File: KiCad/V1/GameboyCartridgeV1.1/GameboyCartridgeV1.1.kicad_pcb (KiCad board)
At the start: 4 copper layers, 52.8 x 61.2 mm, 52 parts, among them J1 USB_C_Receptacle_USB2.0, J2 DBG_UART, J3 Conn_01x06, Q1 CJ2302, SW1 SW_Push, U2 W25Q128JVS, U3 RP2040, U4 CartBus, U5 MCP1825T-3302E/DC, U6 TXB0102DCU, U7 TXB0108PW, U8 TXB0108PW, U9 TXB0108PW, Y1 12MHz

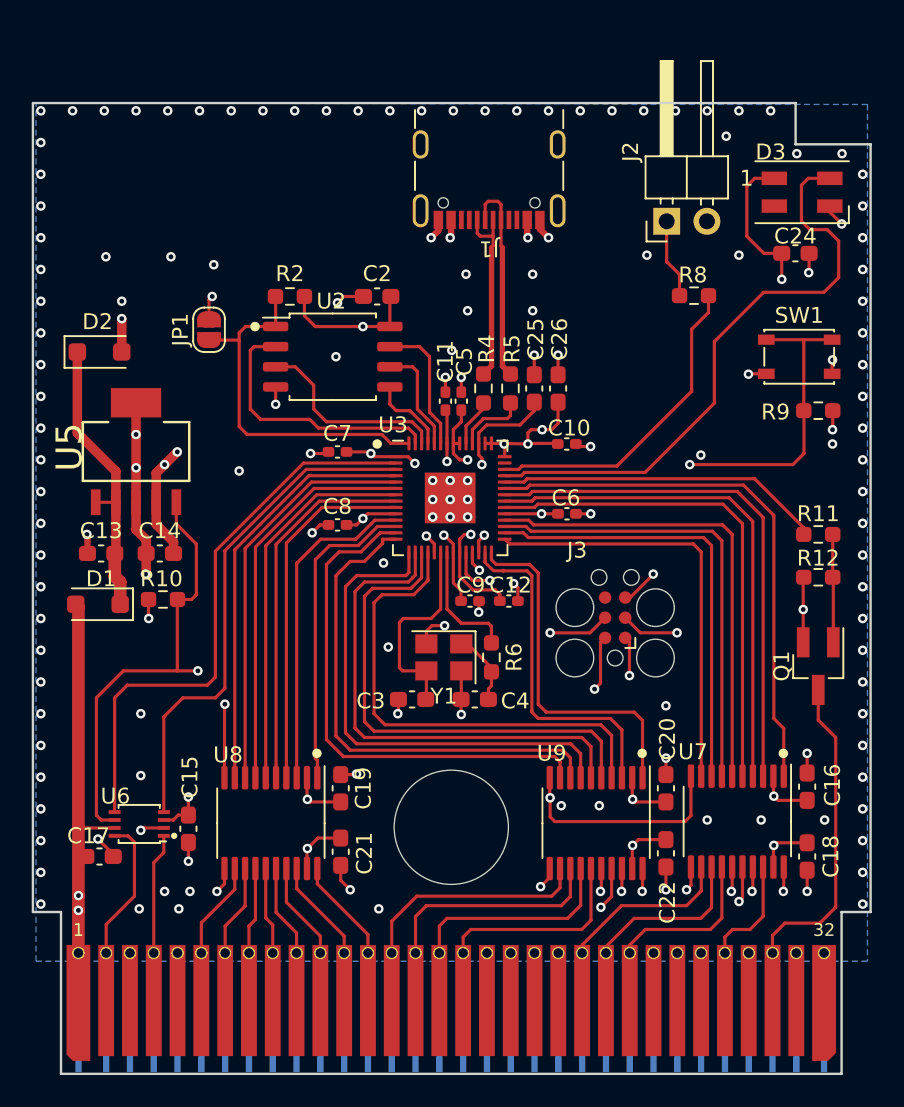
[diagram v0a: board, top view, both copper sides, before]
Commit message: Change folder structure
- Fix Library paths
- Add Libraries
- Add Gerbers, BOM, Position file compatible with JLPCB
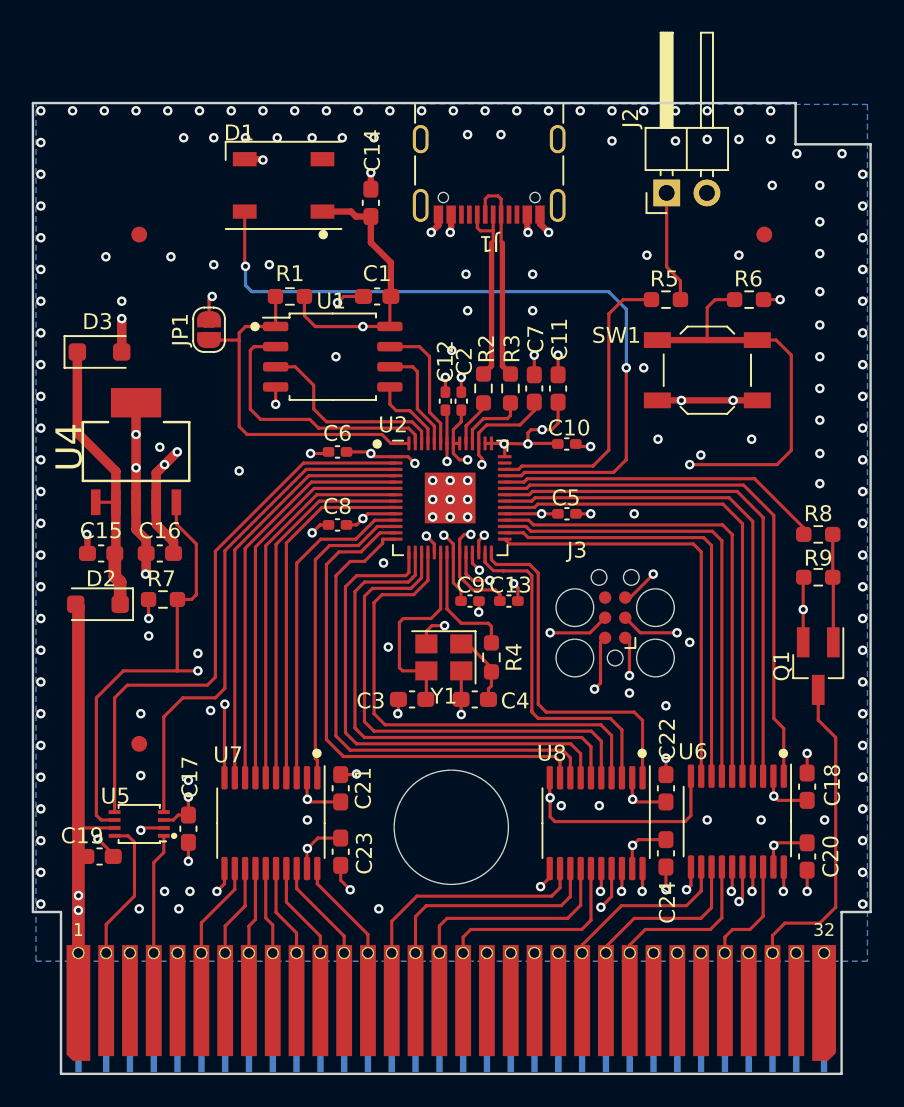
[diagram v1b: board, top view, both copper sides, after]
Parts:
- added FID1: Fiducial, Fiducial:Fiducial_1mm_Mask2mm, F.Cu at (92.1, 64.0)
- added FID2: Fiducial, Fiducial:Fiducial_1mm_Mask2mm, F.Cu at (92.1, 96.1)
- added FID3: Fiducial, Fiducial:Fiducial_1mm_Mask2mm, F.Cu at (131.5, 64.0)
- added G***: LOGO, LOGO, B.Cu at (131.2, 68.9)
- D1: renamed from D3; footprint LED_SMD:LED_SK6812MINI_PLCC4_3.5x3.5mm_P1.75mm -> LED_SMD:LED_WS2812B_PLCC4_5.0x5.0mm_P3.2mm
- SW1: footprint Button_Switch_SMD:SW_SPST_PTS810 -> Button_Switch_SMD:SW_SPST_TL3342
- moved D1 32.7 mm to (101.2, 60.9), turned to 180 degrees
- moved C14 26.9 mm to (106.7, 62.0), turned to -90 degrees
- moved R6 8.25 mm to (130.5, 68.1)
- moved SW1 5.85 mm to (127.9, 72.5)
- moved J2 1.79 mm to (125.3, 61.4)
- moved R5 1.79 mm to (125.3, 68.1), turned to 0 degrees
- moved J1 0.34 mm to (114.2, 59.1)
- renumbered C2 to C1, C26 to C11, C11 to C12, C12 to C13, C24 to C14, C13 to C15, C14 to C16, C15 to C17, C16 to C18, C17 to C19, C5 to C2, C18 to C20, C19 to C21, C20 to C22, C21 to C23, C22 to C24, C6 to C5, C7 to C6, C25 to C7, D1 to D2, D2 to D3, R2 to R1, R4 to R2, R5 to R3, R6 to R4, R8 to R5, R9 to R6, R10 to R7, R11 to R8, R12 to R9, U2 to U1, U3 to U2, U4 to U3, U5 to U4, U6 to U5, U7 to U6, U8 to U7, U9 to U8
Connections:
- U2 pad 41: USB_ID -> unconnected-(U2-GPIO29_ADC3-Pad41)
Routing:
- net LED_DIN: track 37.9 -> 46.9 mm, vias 0 -> 2
- net RST: track 47.7 -> 54.5 mm
- net GND: track 64.7 -> 68.5 mm, vias 156 -> 192
- net Net-(J2-Pin_1): track 5.02 -> 7.08 mm
- net DEBUG_UART_TX: track 20.3 -> 18.7 mm
- net +3V3: track 73.7 -> 72.9 mm, vias 20 -> 19
- net VBUS: track 4.99 -> 4.39 mm
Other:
- board text added: "Croco Cartridge V1.1 11/2023 SQ"
- board text added: "JLCJLCJLCJLC"
- board text removed: "Croco Cartridge V1.1 2023 SQ"
